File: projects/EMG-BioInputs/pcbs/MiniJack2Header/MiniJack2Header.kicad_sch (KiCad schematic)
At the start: 2 parts, among them J1 35RASMT2BHNTRX, J2 901210124

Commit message: refactor: Rename EMG PCB adapter to Header
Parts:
- J1: footprint MiniJack2Jumper:35RASMT2BHNTRX -> MiniJack2Header:35RASMT2BHNTRX; symbol MiniJack2Jumper:35RASMT2BHNTRX -> MiniJack2Header:35RASMT2BHNTRX
- J2: symbol MiniJack2Jumper:901210124 -> MiniJack2Header:901210124
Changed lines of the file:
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@@
 (kicad_sch
-	(version 20231120)
+	(version 20250114)
 	(generator "eeschema")
-	(generator_version "8.0")
+	(generator_version "9.0")
 	(paper "A4")
 	(no_connect
@@
 	)
 	(symbol
-		(lib_id "MiniJack2Jumper:35RASMT2BHNTRX")
+		(lib_id "MiniJack2Header:35RASMT2BHNTRX")
 		(at 144.78 93.98 0)
 		(unit 1)
@@
 			)
 		)
-		(property "Footprint" "MiniJack2Jumper:35RASMT2BHNTRX"
+		(property "Footprint" "MiniJack2Header:35RASMT2BHNTRX"
 			(at 144.78 93.98 0)
 			(effects
@@
 	)
 	(symbol
-		(lib_id "MiniJack2Jumper:901210124")
+		(lib_id "MiniJack2Header:901210124")
 		(at 165.1 91.44 0)
 		(unit 1)
@@
 		)
 	)
+	(embedded_fonts no)
 )

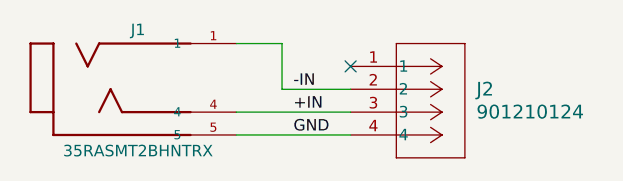
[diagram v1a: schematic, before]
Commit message: fix: Change header pin layout for SensEdu 0.8+
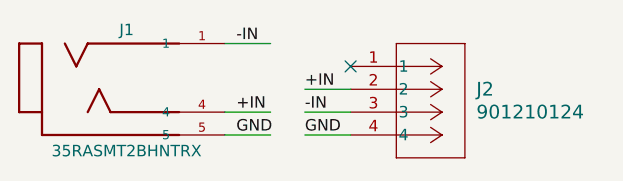
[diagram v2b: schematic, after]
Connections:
- net +IN: now also J2.2; no longer J2.3
- net -IN: now also J2.3; no longer J2.2
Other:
- moved on the sheet: J1
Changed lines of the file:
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@@
 	(wire
 		(pts
-			(xy 152.4 88.9) (xy 157.48 88.9)
+			(xy 151.13 88.9) (xy 156.21 88.9)
 		)
 		(stroke
@@
 	(wire
 		(pts
-			(xy 152.4 96.52) (xy 165.1 96.52)
+			(xy 160.02 93.98) (xy 165.1 93.98)
 		)
 		(stroke
@@
 	(wire
 		(pts
-			(xy 157.48 93.98) (xy 165.1 93.98)
+			(xy 151.13 99.06) (xy 156.21 99.06)
 		)
 		(stroke
@@
 	(wire
 		(pts
-			(xy 157.48 88.9) (xy 157.48 93.98)
+			(xy 160.02 99.06) (xy 165.1 99.06)
 		)
 		(stroke
@@
 	(wire
 		(pts
-			(xy 152.4 99.06) (xy 165.1 99.06)
+			(xy 151.13 96.52) (xy 156.21 96.52)
+		)
+		(stroke
+			(width 0)
+			(type default)
+		)
+	)
+	(wire
+		(pts
+			(xy 160.02 96.52) (xy 165.1 96.52)
 		)
 		(stroke
@@
 	)
 	(label "-IN"
-		(at 158.75 93.98 0)
+		(at 152.4 88.9 0)
+		(effects
+			(font
+				(size 1.27 1.27)
+			)
+			(justify left bottom)
+		)
+	)
+	(label "+IN"
+		(at 160.02 93.98 0)
+		(effects
+			(font
+				(size 1.27 1.27)
+			)
+			(justify left bottom)
+		)
+	)
+	(label "-IN"
+		(at 160.02 96.52 0)
 		(effects
 			(font
@@
 	)
 	(label "GND"
-		(at 158.75 99.06 0)
+		(at 152.4 99.06 0)
+		(effects
+			(font
+				(size 1.27 1.27)
+			)
+			(justify left bottom)
+		)
+	)
+	(label "GND"
+		(at 160.02 99.06 0)
 		(effects
 			(font
@@
 	)
 	(label "+IN"
-		(at 158.75 96.52 0)
+		(at 152.4 96.52 0)
 		(effects
 			(font
@@
 	(symbol
 		(lib_id "MiniJack2Header:35RASMT2BHNTRX")
-		(at 144.78 93.98 0)
+		(at 143.51 93.98 0)
 		(unit 1)
 		(exclude_from_sim no)
@@
 		(dnp no)
 		(property "Reference" "J1"
-			(at 141.478 87.376 0)
+			(at 140.208 87.376 0)
 			(effects
 				(font
@@
 		)
 		(property "Value" "35RASMT2BHNTRX"
-			(at 141.478 100.838 0)
+			(at 140.208 100.838 0)
 			(effects
 				(font
@@
 		)
 		(property "Footprint" "MiniJack2Header:35RASMT2BHNTRX"
-			(at 144.78 93.98 0)
+			(at 143.51 93.98 0)
 			(effects
 				(font
@@
 		)
 		(property "Datasheet" "https://www.switchcraft.com/assets/1/24/35rasmt2bhntrx_cd.pdf?4698"
-			(at 144.78 93.98 0)
+			(at 143.51 93.98 0)
 			(effects
 				(font
@@
 		)
 		(property "Description" ""
-			(at 144.78 93.98 0)
+			(at 143.51 93.98 0)
 			(effects
 				(font
@@
 		)
 		(property "MANUFACTURER" "Switchcraft"
-			(at 144.78 93.98 0)
+			(at 143.51 93.98 0)
 			(effects
 				(font
@@
 		)
 		(property "DigiKey Part Number" "SC1489-1-ND"
-			(at 144.78 93.98 0)
+			(at 143.51 93.98 0)
 			(effects
 				(font
@@
 		)
 		(property "DigiKey Link" "https://www.digikey.at/en/products/detail/switchcraft-inc/35RASMT2BHNTRX/1291178"
-			(at 144.78 93.98 0)
+			(at 143.51 93.98 0)
 			(effects
 				(font
